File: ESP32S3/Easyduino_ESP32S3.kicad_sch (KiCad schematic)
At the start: 33 parts, among them J1 USB_C_Receptacle_USB2.0, J2 USB_C_Receptacle_USB2.0, Q1 Q_NPN_BCE, Q2 Q_NPN_BCE, SW1 SW_Push, SW2 SW_Push, U1 ESP32-S3-WROOM-1, U2 ESP32-S3-DevKitC, U3 CP2102N-Axx-xQFN28, U5 AMS1117-3.3

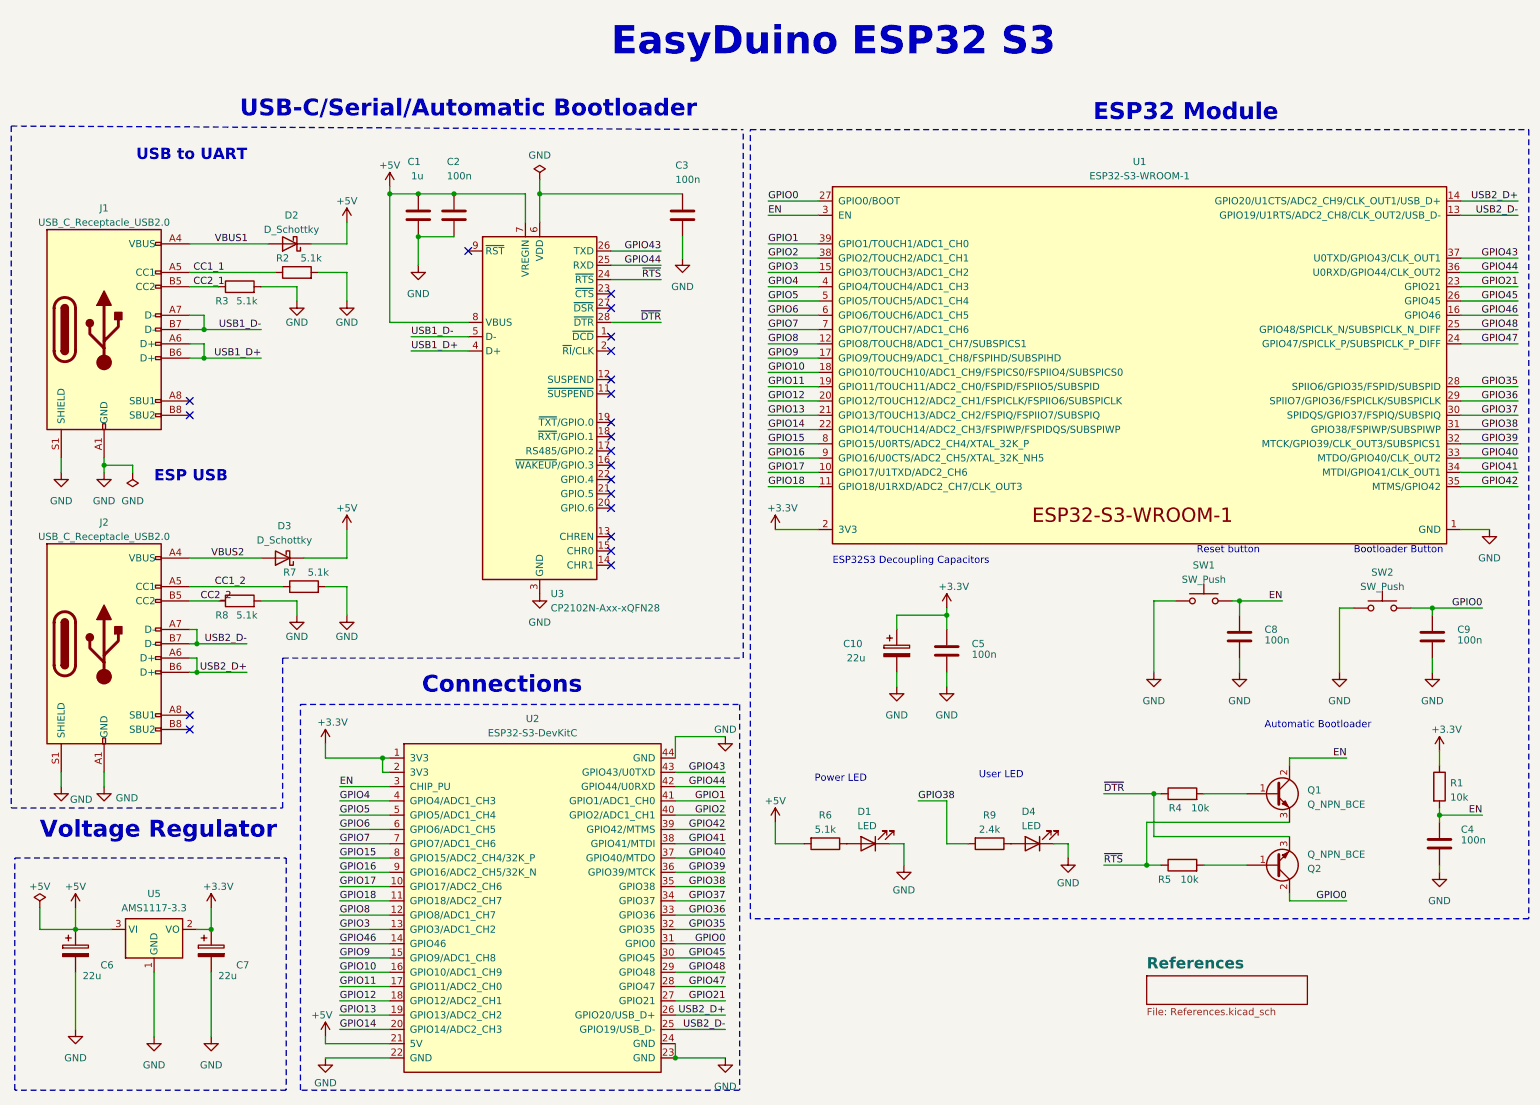
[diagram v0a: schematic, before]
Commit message: ESP32S3 CP2102 bugfix
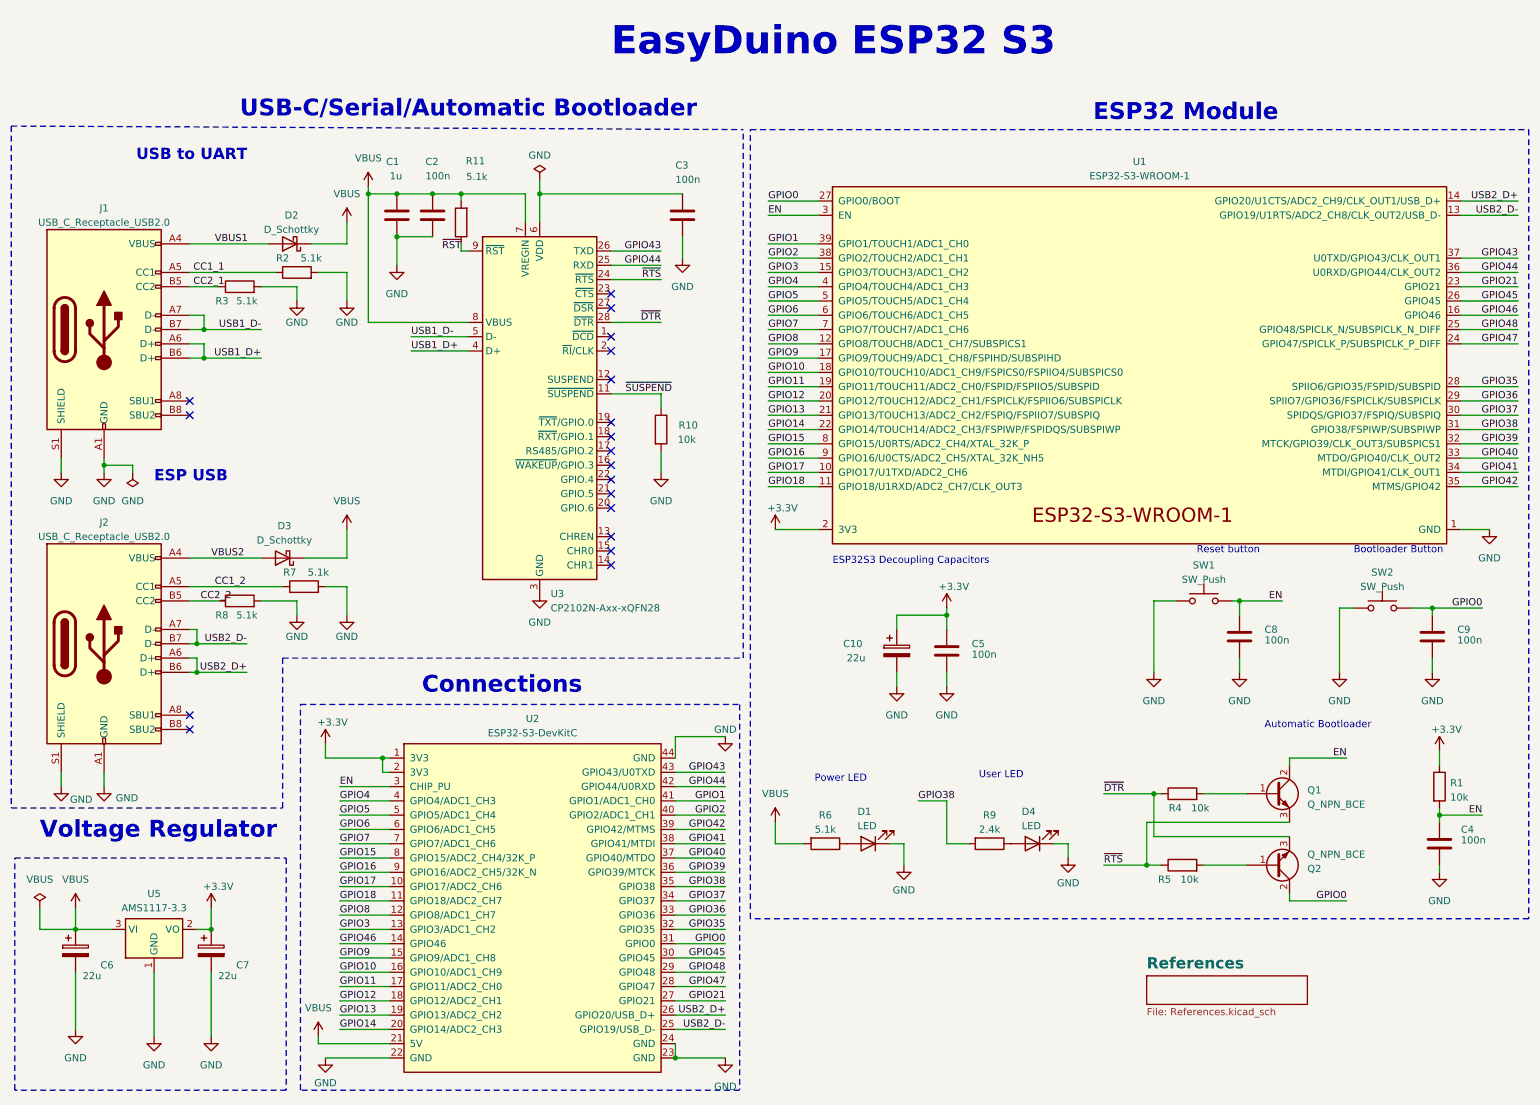
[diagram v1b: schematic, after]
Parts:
- added R10: 10k, Resistor_SMD:R_0402_1005Metric, symbol Device:R
- added R11: 5.1k, Resistor_SMD:R_0402_1005Metric, symbol Device:R
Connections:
- net GND: now also R10.2
- net ~{SUSPEND}: now reaches U3.11 (~{SUSPEND})
- net ~{SUSPEND}: now also R10.1
- net ~{RST}: now reaches U3.9 (~{RST})
- net ~{RST}: now also R11.1
- net +5V renamed VBUS
- net VBUS: now also R11.2
- no-connect marks 21 -> 19
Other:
- moved on the sheet: C1, C2

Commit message: ESP32S3 v1.2
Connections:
- net GPIO43: now also U3.25 (RXD); no longer U3.26 (TXD)
- net GPIO44: now also U3.26 (TXD); no longer U3.25 (RXD)
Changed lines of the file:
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@@
+		)
+	)
+	(label "GPIO44"
+		(at 129.54 43.18 180)
+		(effects
+			(font
+				(size 1.27 1.27)
+			)
+			(justify right bottom)
 		)
 	)
@@
 		)
 	)
-	(label "GPIO43"
-		(at 129.54 43.18 180)
-		(effects
-			(font
-				(size 1.27 1.27)
-			)
-			(justify right bottom)
-		)
-	)
 	(label "GPIO3"
 		(at 72.39 163.83 0)
@@
 		)
 	)
-	(label "GPIO44"
+	(label "GPIO43"
 		(at 129.54 45.72 180)
 		(effects
